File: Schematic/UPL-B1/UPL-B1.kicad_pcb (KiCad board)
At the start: 2 copper layers, 155 x 130 mm, 302 parts, among them K2 G5V-2_Split, P20 TestPoint, P21 TestPoint, P30 TestPoint, P31 TestPoint, P32 TestPoint, P33 TestPoint, P34 TestPoint, P40 TestPoint, P53 TestPoint, P54 TestPoint, P55 TestPoint, P56 TestPoint, P57 TestPoint, P58 TestPoint, X1 5102159-8, X2 Conn_01x03_Pin_Bridge, X3 Conn_01x06_Pin, X4 Conn_01x06_Pin, X50 Conn_01x03_Pin_Bridge, X51 Conn_01x03_Pin_Bridge, X52 Conn_01x03_Pin_Bridge

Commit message: Rough component outline on PCB
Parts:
- C208, C209, C210, C308, C406, C408, C511, C518, N55, R206, R326, R335, R344, R348, R401, R519, R535, R538, R543, V315, V401, V403, V507, V515: moved to B.Cu
- C302, C402: footprint Capacitor_THT:C_Axial_L22.0mm_D9.5mm_P27.50mm_Horizontal -> Capacitor_THT:C_Axial_L17.0mm_D7.0mm_P25.00mm_Horizontal
- R503: footprint Resistor_THT:R_Axial_DIN0204_L3.6mm_D1.6mm_P7.62mm_Horizontal -> Resistor_SMD:R_1206_3216Metric_Pad1.30x1.75mm_HandSolder
- R541: footprint Resistor_THT:R_Axial_DIN0204_L3.6mm_D1.6mm_P7.62mm_Horizontal -> Resistor_SMD:R_1206_3216Metric_Pad1.30x1.75mm_HandSolder; moved to B.Cu
- moved V315 289.9 mm to (127.6, 39.6), turned to 180 degrees
- moved C408 282.9 mm to (162.6, 144.4), turned to 180 degrees
- moved C414 263.0 mm to (154.5, 65.9)
- moved C406 262.7 mm to (142.2, 71.9), turned to 180 degrees
- moved V403 261.9 mm to (145.9, 92.4), turned to 180 degrees
- moved V401 260.7 mm to (145.2, 86.9), turned to 180 degrees
- moved C308 254.2 mm to (126.5, 144.3), turned to 180 degrees
- moved R401 245.2 mm to (132.6, 85.5), turned to 180 degrees
- moved R326 242.6 mm to (135.3, 63.8), turned to 180 degrees
- moved V507 238.9 mm to (77.0, 48.8), turned to 180 degrees
- moved R344 232.9 mm to (126.8, 116.8), turned to -90 degrees
- moved X51 232.0 mm to (87.7, 70.0)
- moved R404 231.2 mm to (147.7, 81.5)
- moved R403 231.1 mm to (147.7, 79.2)
- moved R402 231.1 mm to (147.7, 76.9)
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
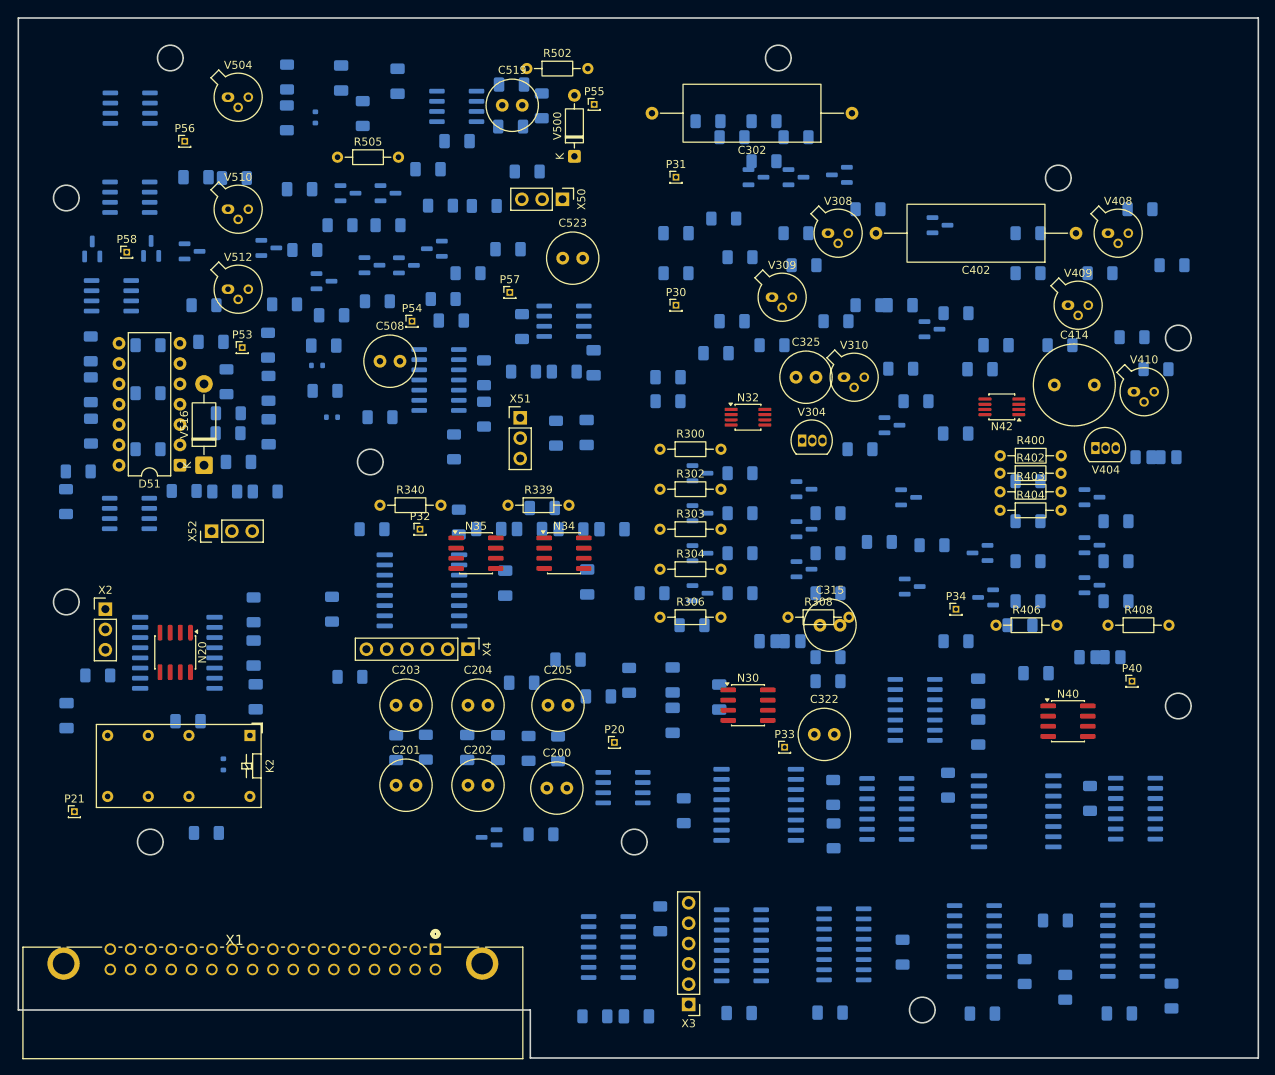
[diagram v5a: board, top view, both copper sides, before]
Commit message: Updated PCB layout to include copper zones
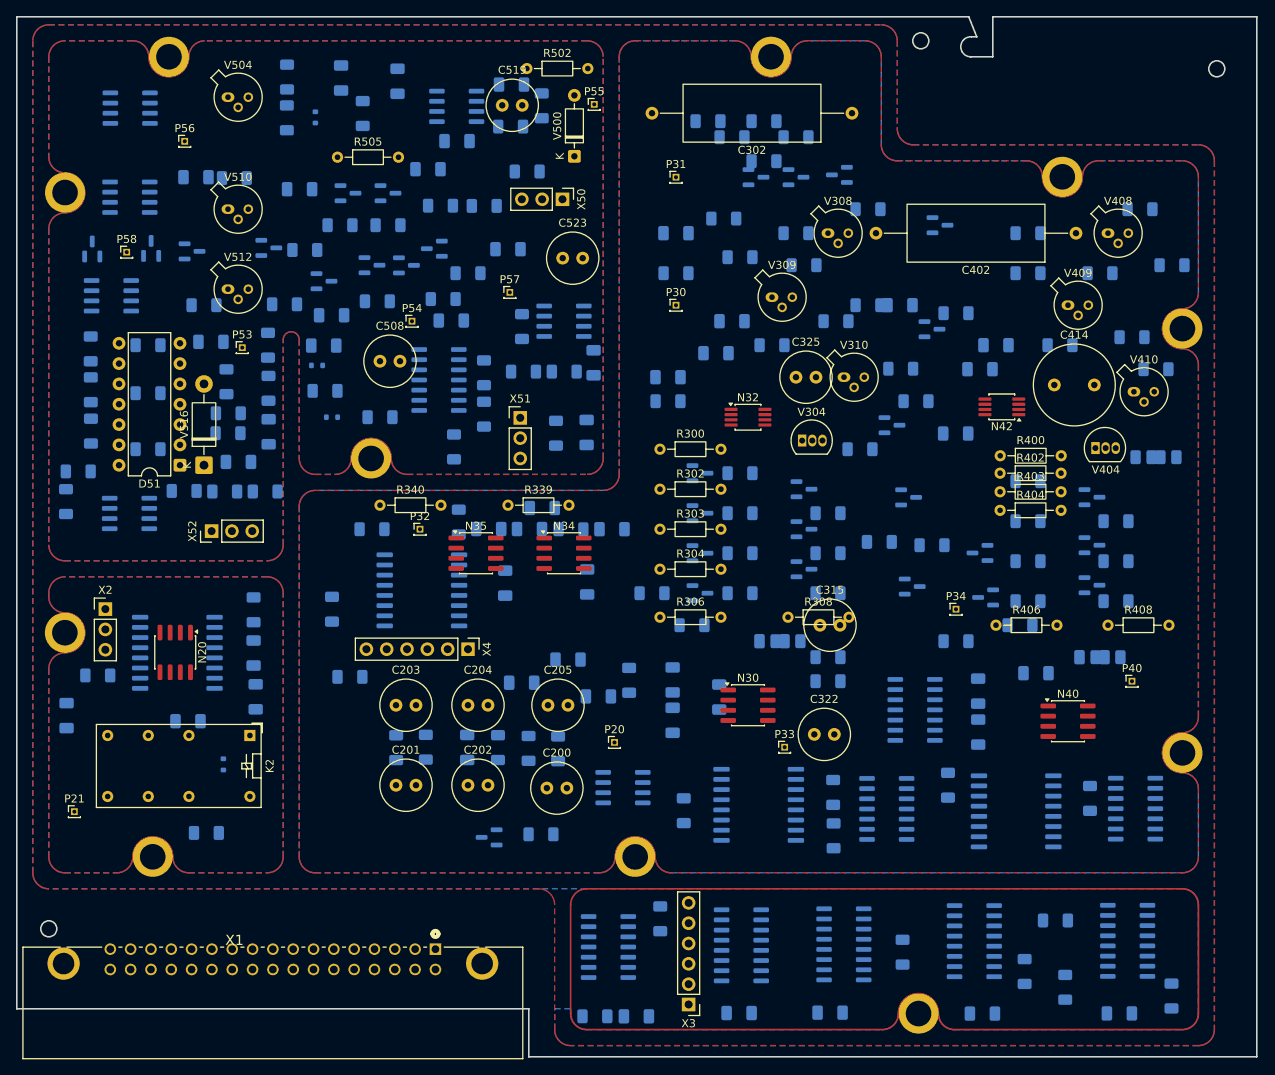
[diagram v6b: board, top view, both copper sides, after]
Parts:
- added ?: , , F.Cu at (170.5, 58.8)
- added ?: , , F.Cu at (170.5, 111.9)
- added ?: , , F.Cu at (41.8, 124.8)
- added ?: , , F.Cu at (119.1, 24.8)
- added ?: , , F.Cu at (102.1, 124.9)
- added ?: , , F.Cu at (137.5, 144.4)
- added ?: , , F.Cu at (30.8, 96.8)
- added ?: , , F.Cu at (155.5, 39.9)
- added ?: , , F.Cu at (69.1, 75.1)
- added ?: , , F.Cu at (43.8, 24.9)
- added ?: , , F.Cu at (30.8, 41.8)
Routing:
- added copper zone on B.Cu, net GNDD
- added copper zone on F.Cu, net GNDD
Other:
- outline, holes or cut-outs redrawn
- copper layers 2 -> 4
- board text added: "Import Solder Mask (No grouping) Import Copper Layer (No grouping) Set Zone and explude inner grids from filling"

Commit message: update on PCB board
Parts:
- added G***: LOGO, UPL_B1:BVKSound_Logo, F.Cu at (166.2, 31.6)
- added REF**: Logo, UPL_B1:Logo Peter, F.Cu at (174.2, 36.5)
- moved X51 3.80 mm to (87.7, 73.8), turned to 180 degrees
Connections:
- ? pad 1: (no net) -> GNDD (x11)
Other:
- board text added: "1) Import Graphics for Edge Outline WITH grouping 2) Import Graphics for Cu Top Zone WITHOUT grouping 3) Convert Layer into Zone attached to GND with Priority 10 4) Import Graphics for Solder Mask Top Zone WITHOUT grouping 5) Convert Layer into Zone (make sure the solder mask zone is selected before doing this) 6) Import Graphics for Rule WITHOUT grouping (add in a user layer) 7) Convert into Rul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"
- board text added: "LOW DIST. GENERATOR"
- board text added: "OPEN UPL-B1 REV1.0 2025"
- board text removed: "Import Solder Mask (No grouping) Import Copper Layer (No grouping) Set Zone and explude inner grids from filling"

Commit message: rough part outline
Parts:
- moved R348 80.8 mm to (121.3, 106.4), turned to 0 degrees
- moved V315 14.4 mm to (113.4, 41.9), turned to -90 degrees
- moved R502 14.1 mm to (74.5, 27.0), turned to 180 degrees
- moved R535 11.9 mm to (42.6, 83.1), turned to -90 degrees
- moved N40 9.61 mm to (152.1, 99.2), turned to 180 degrees
- moved N30 9.36 mm to (109.7, 99.1), turned to 180 degrees
- moved R335 9.24 mm to (114.9, 36.0)
- moved P32 8.95 mm to (66.6, 86.4)
- moved R308 8.61 mm to (118.3, 103.0), turned to 90 degrees
- moved V402 8.13 mm to (143.3, 86.3), turned to 90 degrees
- moved R401 7.95 mm to (138.4, 80.0), turned to 90 degrees
- moved C211 7.69 mm to (41.3, 113.8), turned to 180 degrees
- moved V400 7.32 mm to (143.3, 77.9), turned to 90 degrees
- moved R408 7.10 mm to (162.7, 102.8), turned to 90 degrees
- moved R319 6.95 mm to (129.2, 85.6)
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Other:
- board text added: "+2V5"
- board text added: "-6V2"
- board text added: "COS"
- board text added: "ENAB +6V -24V -15V +15V +5V"
- board text added: "SD0 SD1 CLK /RD /WR WR"
- board text added: "SIN"
